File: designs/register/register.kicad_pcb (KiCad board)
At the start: 2 copper layers, 100 x 100 mm, 121 parts, among them J101 Conn_01x08, J102 Conn_01x02_Power, J103 Conn_01x08, J104 Conn_01x01, J105 Conn_01x01, J106 Conn_01x08, J107 Conn_01x08, J108 Conn_01x08, J109 Conn_01x01, Q101 2N7000, Q102 2N7000, Q103 BC547, Q104 2N7000, Q105 2N7000, Q106 2N7000, Q107 2N7000, Q108 2N7000, Q109 2N7000, Q110 2N7000, Q111 2N7000, Q112 2N7000, Q113 2N7000, Q114 2N7000, Q115 2N7000, Q116 2N7000, Q117 2N7000, Q118 2N7000, Q119 2N7000, Q120 2N7000, Q121 2N7000, Q201 2N7000, Q202 2N7000, Q203 2N7000, Q204 2N7000, Q205 2N7000, Q206 2N7000, Q207 2N7000, Q301 2N7000, Q302 2N7000, Q303 2N7000, Q304 2N7000, Q305 2N7000, Q306 2N7000, Q307 2N7000, Q401 2N7000, Q402 2N7000, Q403 2N7000, Q404 2N7000, Q405 2N7000, Q406 2N7000, Q407 2N7000, Q501 2N7000, Q502 2N7000, Q503 2N7000, Q504 2N7000, Q505 2N7000, Q506 2N7000, Q507 2N7000, Q601 2N7000, Q602 2N7000, Q603 2N7000, Q604 2N7000, Q605 2N7000, Q606 2N7000, Q607 2N7000, Q701 2N7000, Q702 2N7000, Q703 2N7000, Q704 2N7000, Q705 2N7000, Q706 2N7000, Q707 2N7000, Q801 2N7000, Q802 2N7000, Q803 2N7000, Q804 2N7000, Q805 2N7000, Q806 2N7000, Q807 2N7000, Q901 2N7000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

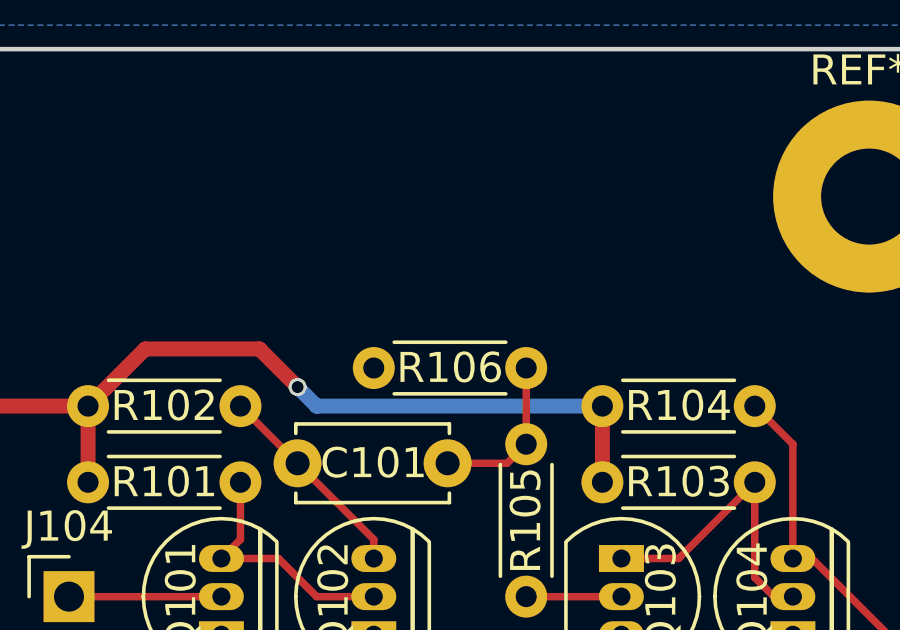
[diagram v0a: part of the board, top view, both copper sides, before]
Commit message: Updated register design to fix small flaw.
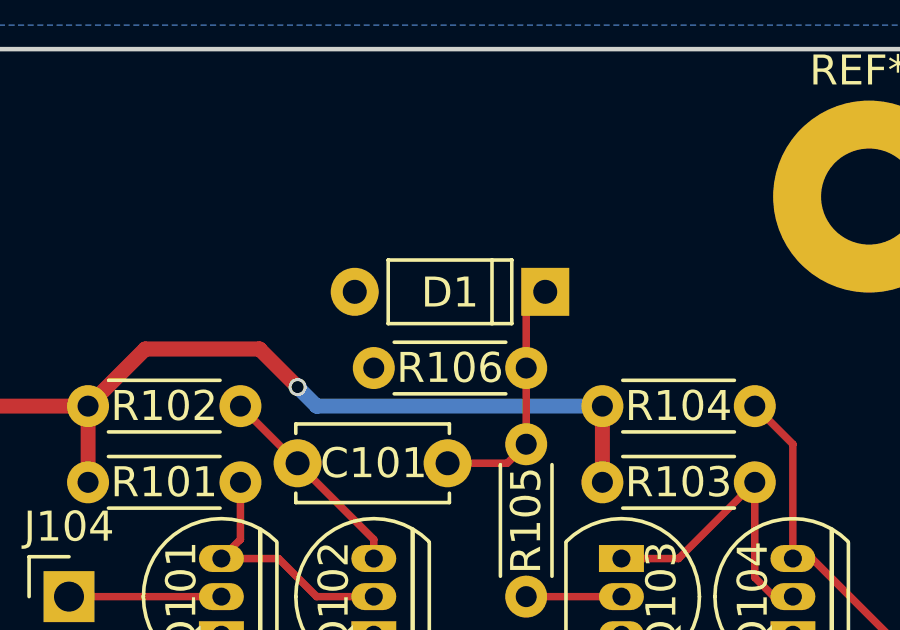
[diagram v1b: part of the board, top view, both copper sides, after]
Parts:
- added D1: 1N4148, footprints:D_default, F.Cu at (125.7, 23.5)
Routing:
- net Net-(C101-Pad2): track 5.42 -> 8.23 mm
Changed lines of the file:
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@@
-(kicad_pcb (version 4) (host pcbnew 4.0.7-e2-6376~58~ubuntu16.04.1)
+(kicad_pcb (version 4) (host pcbnew 4.0.7-e2-6376~61~ubuntu18.04.1)
   (general
-    (links 262)
+    (links 264)
     (no_connects 0)
-    (area 40.64 20.32 142.240001 110.490001)
+    (area 35.012143 14.605 147.867858 116.205001)
     (thickness 1.6)
     (drawings 4)
-    (tracks 581)
+    (tracks 583)
     (zones 0)
-    (modules 121)
+    (modules 122)
     (nets 77)
   )
@@
     (pad 1 thru_hole circle (at 0 0) (size 6.4 6.4) (drill 3.2) (layers *.Cu *.Mask))
   )
+  (module footprints:D_default (layer F.Cu)
+    (at 125.73 23.495 180)
+    (descr "D, DO-35_SOD27 series, Axial, Horizontal, pin pitch=7.62mm, , length*diameter=4*2mm^2, , http://www.diodes.com/_files/packages/DO-35.pdf")
+    (tags "D DO-35_SOD27 series Axial Horizontal pin pitch 7.62mm  length 4mm diameter 2mm")
+    (fp_text reference D1 (at 3.175 -0.028 180) (layer F.SilkS)
+      (effects (font (size 1 1) (thickness 0.15)))
+    )
+    (fp_text value 1N4148 (at 3.81 2.06 180) (layer F.Fab)
+      (effects (font (size 1 1) (thickness 0.15)))
+    )
+    (fp_text user %R (at 3.175 0 180) (layer F.Fab)
+      (effects (font (size 1 1) (thickness 0.15)))
+    )
+    (fp_line (start 1.175 -1) (end 1.175 1) (layer F.Fab) (width 0.1))
+    (fp_line (start 1.175 1) (end 5.175 1) (layer F.Fab) (width 0.1))
+    (fp_line (start 5.175 1) (end 5.175 -1) (layer F.Fab) (width 0.1))
+    (fp_line (start 5.175 -1) (end 1.175 -1) (layer F.Fab) (width 0.1))
+    (fp_line (start 1.775 -1) (end 1.775 1) (layer F.Fab) (width 0.1))
+    (fp_line (start 1.115 -1.06) (end 1.115 1.06) (layer F.SilkS) (width 0.12))
+    (fp_line (start 1.115 1.06) (end 5.235 1.06) (layer F.SilkS) (width 0.12))
+    (fp_line (start 5.235 1.06) (end 5.235 -1.06) (layer F.SilkS) (width 0.12))
+    (fp_line (start 5.235 -1.06) (end 1.115 -1.06) (layer F.SilkS) (width 0.12))
+    (fp_line (start 1.775 -1.06) (end 1.775 1.06) (layer F.SilkS) (width 0.12))
+    (fp_line (start -1.05 -1.35) (end -1.05 1.35) (layer F.CrtYd) (width 0.05))
+    (fp_line (start -1.05 1.35) (end 7.375 1.35) (layer F.CrtYd) (width 0.05))
+    (fp_line (start 7.3792 1.35) (end 7.3792 -1.35) (layer F.CrtYd) (width 0.05))
+    (fp_line (start 7.375 -1.35) (end -1.05 -1.35) (layer F.CrtYd) (width 0.05))
+    (pad 1 thru_hole rect (at 0 0 180) (size 1.6 1.6) (drill 0.8) (layers *.Cu *.Mask)
+      (net 2 "Net-(C101-Pad2)"))
+    (pad 2 thru_hole oval (at 6.35 0 180) (size 1.6 1.6) (drill 0.8) (layers *.Cu *.Mask)
+      (net 12 GND))
+    (model ${KISYS3DMOD}/Diodes_THT.3dshapes/D_DO-35_SOD27_P7.62mm_Horizontal.wrl
+      (at (xyz 0 0 0))
+      (scale (xyz 0.393701 0.393701 0.393701))
+      (rotate (xyz 0 0 0))
+    )
+  )
   (gr_line (start 41.44 115.405) (end 41.44 15.405) (angle 90) (layer Edge.Cuts) (width 0.15))
   (gr_line (start 141.44 115.405) (end 41.44 115.405) (angle 90) (layer Edge.Cuts) (width 0.15))
@@
   (segment (start 117.475 29.21) (end 120.015 31.75) (width 0.25) (layer F.Cu) (net 1))
   (segment (start 120.015 31.75) (end 120.015 32.385) (width 0.25) (layer F.Cu) (net 1))
+  (segment (start 125.095 26.035) (end 125.095 24.13) (width 0.25) (layer F.Cu) (net 2))
+  (segment (start 125.095 24.13) (end 125.73 23.495) (width 0.25) (layer F.Cu) (net 2))
   (segment (start 125.095 28.575) (end 125.095 26.035) (width 0.25) (layer F.Cu) (net 2))
   (segment (start 122.475 29.21) (end 124.46 29.21) (width 0.25) (layer F.Cu) (net 2))
